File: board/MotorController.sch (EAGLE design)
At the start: 33 parts, among them Q1 IPP80P03P4L-04, Q2 8Mhz, T1 BT139X-600E, U1 ATTINY84-20PU

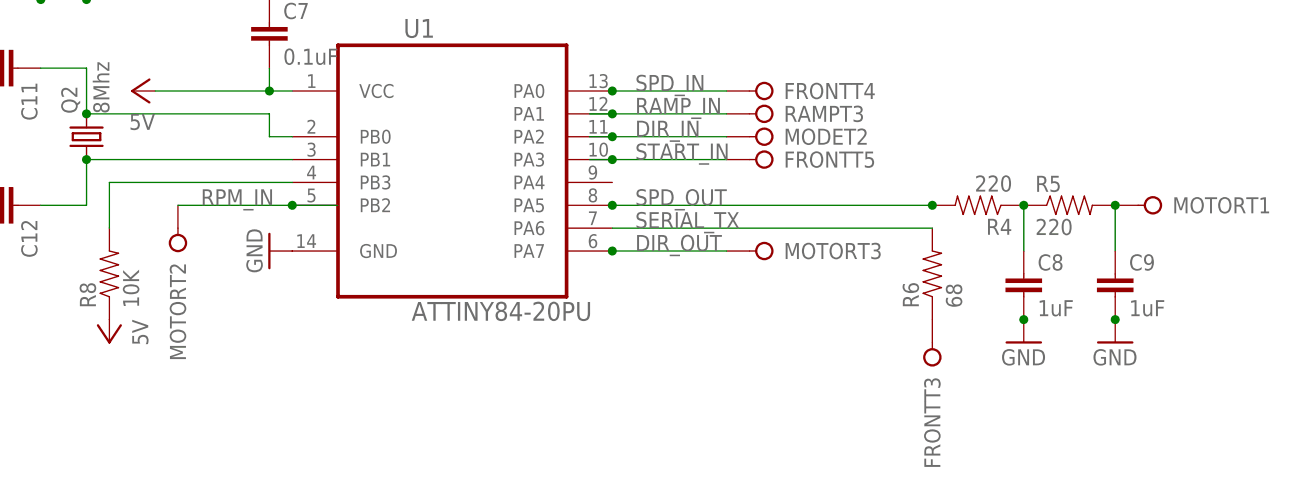
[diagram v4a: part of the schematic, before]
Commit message: Board layout improvements
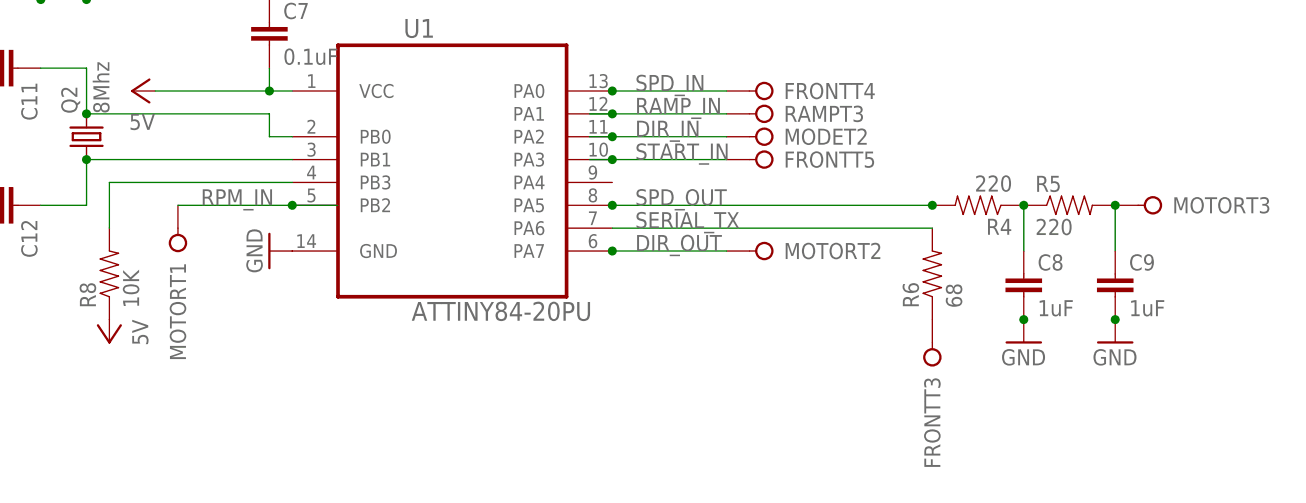
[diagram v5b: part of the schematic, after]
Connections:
- net N$2 renamed RESET
- net DIR_OUT: now also MOTORT2.KL; no longer MOTORT3.KL
- net N$10: now also MOTORT3.KL; no longer MOTORT1.KL
- net RPM_IN: now also MOTORT1.KL; no longer MOTORT2.KL
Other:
- moved on the sheet: MOTORT1, MOTORT2, MOTORT3
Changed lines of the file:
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@@
 <instance part="FRONT" gate="T3" x="106.68" y="-17.78" rot="R90"/>
 <instance part="RAMP" gate="T3" x="88.9" y="10.16" rot="R180"/>
-<instance part="MOTOR" gate="T1" x="132.08" y="0" rot="R180"/>
-<instance part="MOTOR" gate="T2" x="22.86" y="-5.08" rot="R90"/>
-<instance part="MOTOR" gate="T3" x="88.9" y="-5.08" rot="R180"/>
 <instance part="FRONT" gate="T4" x="88.9" y="12.7" rot="R180"/>
 <instance part="FRONT" gate="T5" x="88.9" y="5.08" rot="R180"/>
@@
 <instance part="MOTOR" gate="T4" x="63.5" y="35.56" rot="R90"/>
 <instance part="C1" gate="G$1" x="40.64" y="48.26"/>
+<instance part="MOTOR" gate="T1" x="22.86" y="-5.08" rot="R90"/>
+<instance part="MOTOR" gate="T2" x="88.9" y="-5.08" rot="R180"/>
+<instance part="MOTOR" gate="T3" x="132.08" y="0" rot="R180"/>
 </instances>
 <busses>
@@
 <junction x="35.56" y="0"/>
 <label x="25.4" y="0" size="1.778" layer="95"/>
-<pinref part="MOTOR" gate="T2" pin="KL"/>
+<pinref part="MOTOR" gate="T1" pin="KL"/>
 </segment>
 </net>
@@
 <label x="73.66" y="-5.08" size="1.778" layer="95"/>
 <junction x="71.12" y="-5.08"/>
-<pinref part="MOTOR" gate="T3" pin="KL"/>
+<pinref part="MOTOR" gate="T2" pin="KL"/>
 </segment>
 </net>
@@
 <pinref part="C9" gate="G$1" pin="1"/>
 <wire x1="127" y1="-5.08" x2="127" y2="0" width="0.1524" layer="91"/>
-<pinref part="MOTOR" gate="T1" pin="KL"/>
+<pinref part="MOTOR" gate="T3" pin="KL"/>
 <junction x="127" y="0"/>
 </segment>
@@
 </segment>
 </net>
-<net name="N$2" class="0">
+<net name="RESET" class="0">
 <segment>
 <pinref part="U1" gate="A" pin="PB3"/>

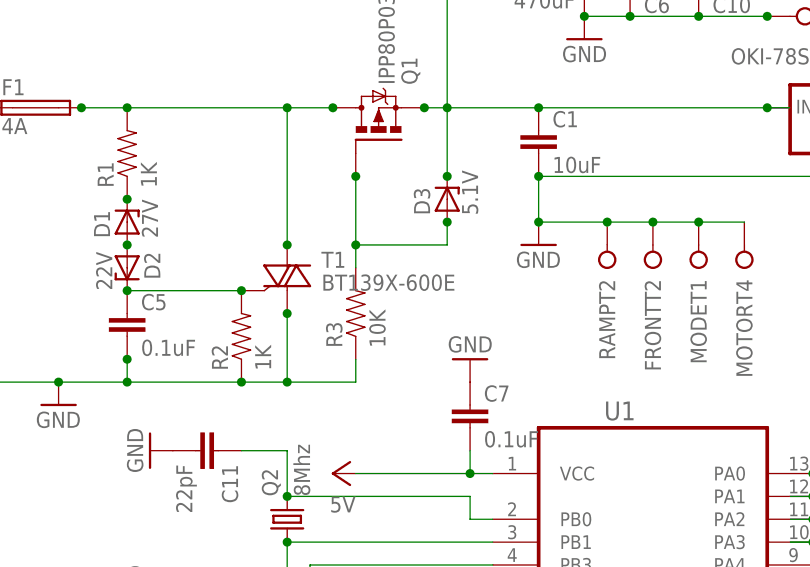
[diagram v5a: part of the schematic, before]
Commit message: Change triac value
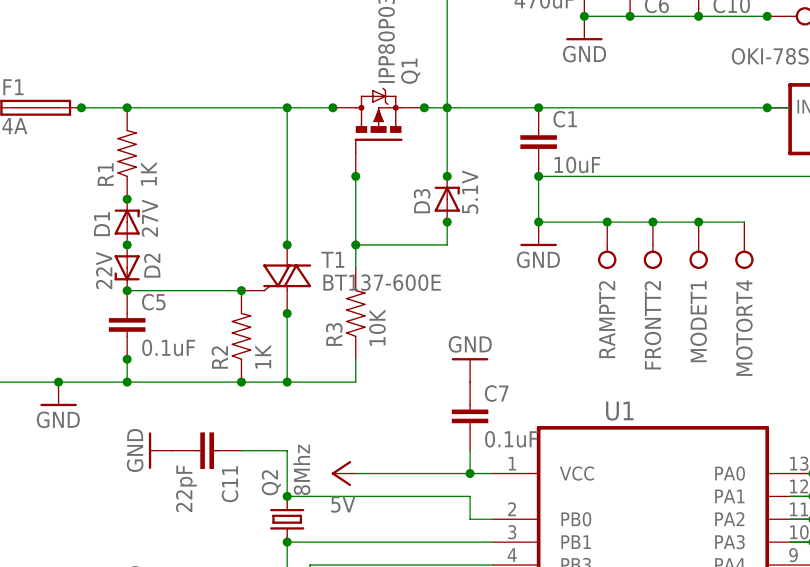
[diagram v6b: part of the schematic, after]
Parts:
- T1: value BT139X-600E -> BT137-600E
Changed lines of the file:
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@@
 <part name="C4" library="SaintGimp" deviceset="CAP-POL" device="-25-14" value="470uF"/>
 <part name="F1" library="SaintGimp" deviceset="FUSE" device="" value="4A"/>
-<part name="T1" library="SaintGimp" deviceset="TRIAC" device="-H" value="BT139X-600E"/>
+<part name="T1" library="SaintGimp" deviceset="TRIAC" device="-H" value="BT137-600E"/>
 <part name="D2" library="SaintGimp" deviceset="ZENER" device="-7.5" value="22V"/>
 <part name="D1" library="SaintGimp" deviceset="ZENER" device="-7.5" value="27V"/>

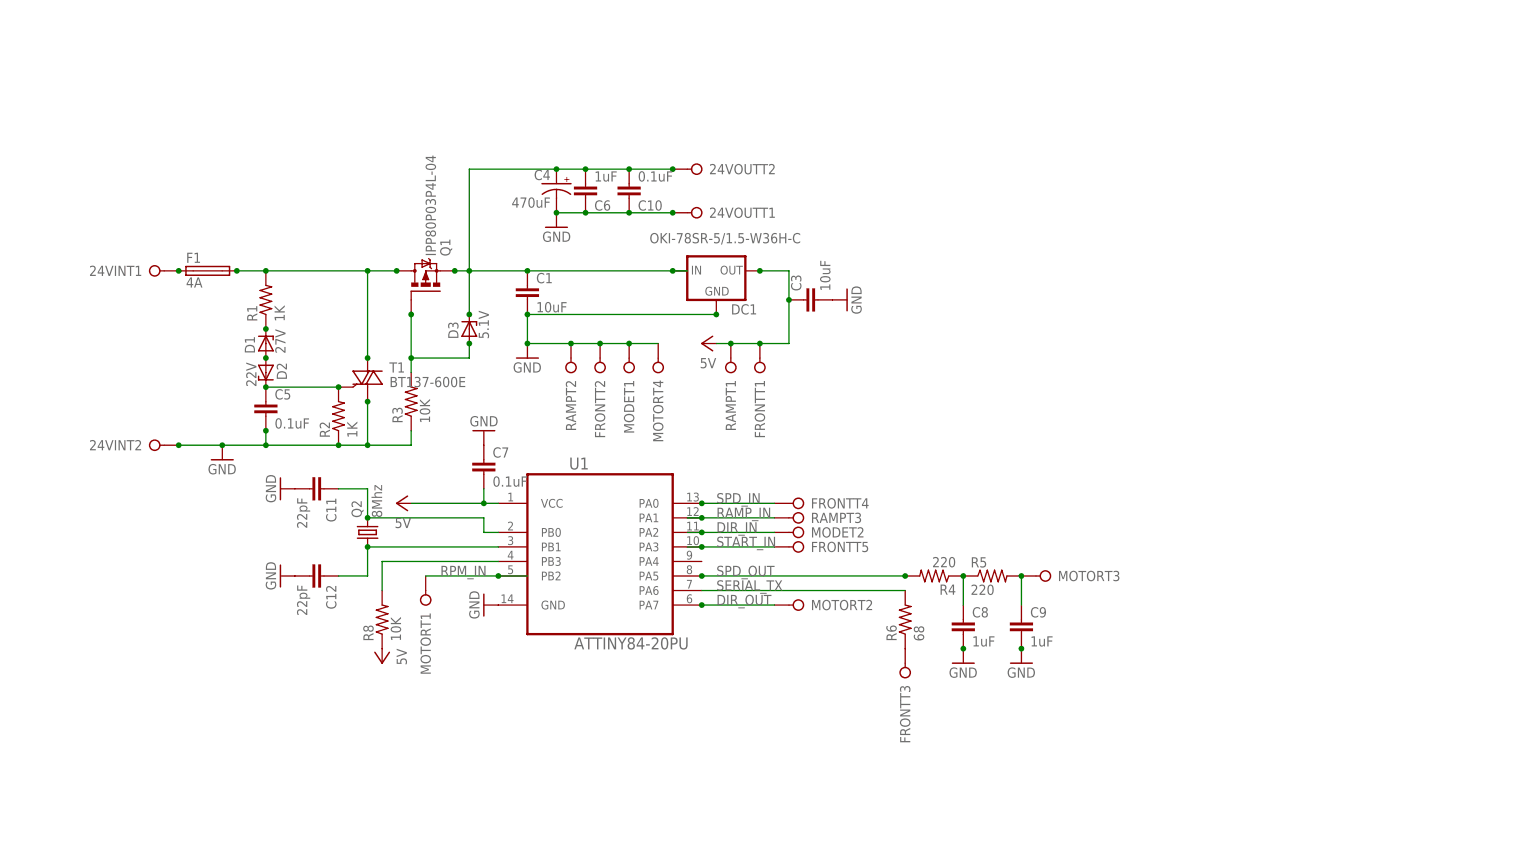
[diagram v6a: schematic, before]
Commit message: Switch to pin headers and ATMega328P
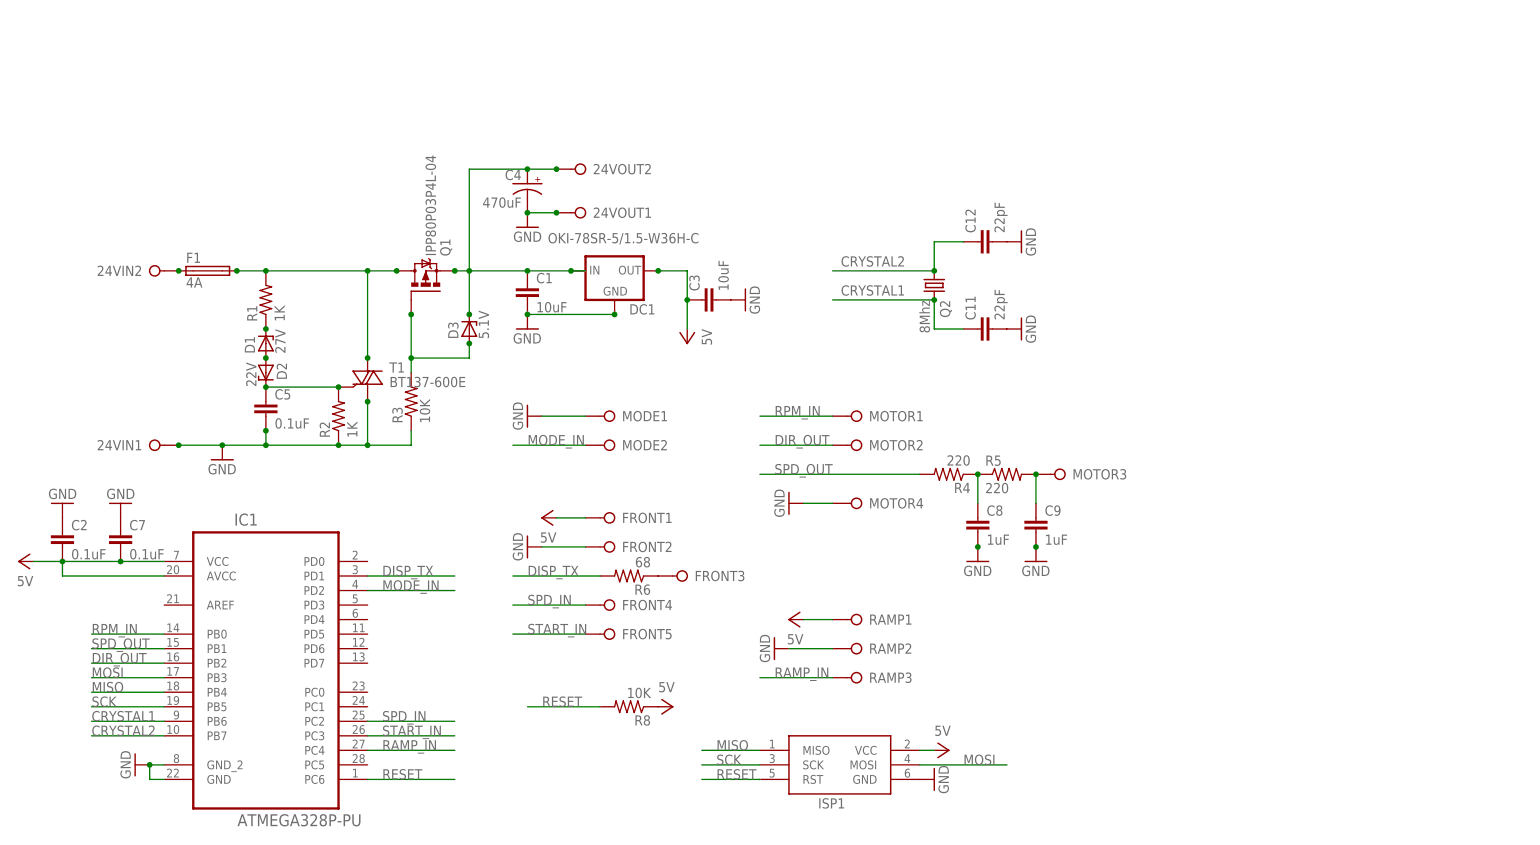
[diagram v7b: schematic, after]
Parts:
- removed C10: 0.1uF, SaintGimp:CAPACITOR-5MM
- removed C6: 1uF, SaintGimp:CAPACITOR-5MM
- removed U1: ATTINY84-20PU, SaintGimp:ATTINY84-20PU
- added C2: 0.1uF, SaintGimp:CAPACITOR-5MM
- added IC1: ATMEGA328P-PU, SaintGimp:ATMEGA328P-PU
- added ISP1: ICSP-HEADER-6, SaintGimp:ICSP-HEADER-6
- 24VIN, 24VOUT, MODE: value SCREW-TERM-2 -> PINHD-1X2; device SaintGimp:SCREW-TERM-2 -> SaintGimp:PINHD-1X2
- FRONT: value SCREW-TERM-5 -> PINHD-1X5; device SaintGimp:SCREW-TERM-5 -> SaintGimp:PINHD-1X5
- MOTOR: value SCREW-TERM-4 -> PINHD-1X4; device SaintGimp:SCREW-TERM-4 -> SaintGimp:PINHD-1X4
- RAMP: value SCREW-TERM-3 -> PINHD-1X3; device SaintGimp:SCREW-TERM-3 -> SaintGimp:PINHD-1X3
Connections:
- removed net DIR_IN: MODET2.KL, U1.PA2
- removed net N$12: C12.1, Q2.1, U1.PB1
- removed net N$13: C11.1, Q2.2, U1.PB0
- removed net SERIAL_TX: R6.2, U1.PA6
- new net CRYSTAL1: C11.1, IC1.PB6, Q2.2
- new net CRYSTAL2: C12.1, IC1.PB7, Q2.1
- new net DISP_TX: IC1.PD1, R6.2
- new net MISO: IC1.PB4, ISP1.MISO
- new net MODE_IN: IC1.PD2, MODE2.KL
- new net MOSI: IC1.PB3, ISP1.MOSI
- new net SCK: IC1.PB5, ISP1.SCK
- net 24V-PROTECTED: now also 24VOUT2.KL; no longer 24VOUTT2.KL, C10.2, C6.2
- net DIR_OUT: now also IC1.PB2, MOTOR2.KL; no longer MOTORT2.KL, U1.PA7
- net GND: now also 24VIN1.KL, 24VOUT1.KL, C2.1, FRONT2.KL, IC1.GND, IC1.GND_2, ISP1.GND, MODE1.KL, MOTOR4.KL, RAMP2.KL; no longer 24VINT2.KL, 24VOUTT1.KL, C10.1, C6.1, FRONTT2.KL, MODET1.KL, MOTORT4.KL, RAMPT2.KL, U1.GND
- net N$10: now also MOTOR3.KL; no longer MOTORT3.KL
- net N$3: now also 24VIN2.KL; no longer 24VINT1.KL
- net N$8: now also FRONT3.KL; no longer FRONTT3.KL
- net RAMP_IN: now also IC1.PC4, RAMP3.KL; no longer RAMPT3.KL, U1.PA1
- net RESET: now also IC1.PC6, ISP1.RST; no longer U1.PB3
- net RPM_IN: now also IC1.PB0, MOTOR1.KL; no longer MOTORT1.KL, U1.PB2
- net SPD_IN: now also FRONT4.KL, IC1.PC2; no longer FRONTT4.KL, U1.PA0
- net SPD_OUT: now also IC1.PB1; no longer U1.PA5
- net START_IN: now also FRONT5.KL, IC1.PC3; no longer FRONTT5.KL, U1.PA3
- net VCC: now also C2.2, FRONT1.KL, IC1.AVCC, IC1.VCC, ISP1.VCC, RAMP1.KL; no longer FRONTT1.KL, RAMPT1.KL, U1.VCC
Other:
- moved on the sheet: C11, C12, C3, C4, C7, C8, C9, DC1, Q2, R4, R5, R6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

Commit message: Version 3, many changes
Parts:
- added FOOT: PINHD-1X2BIG, SaintGimp:PINHD-1X2BIG
- added SIDE_EXP: PINHD-1X3BIG, SaintGimp:PINHD-1X3BIG
- 24VIN, 24VOUT, MODE: value PINHD-1X2 -> PINHD-1X2BIG; device SaintGimp:PINHD-1X2 -> SaintGimp:PINHD-1X2BIG
- C11, C12: value 22pF -> 20pF
- C2, C5, C7, C8, C9: device SaintGimp:CAPACITOR-5MM -> SaintGimp:CAPACITOR-2.5MM
- C4: value 470uF -> 1000uF
- D3: value 5.1V -> 10V
- FRONT: value PINHD-1X5 -> PINHD-1X7BIG; device SaintGimp:PINHD-1X5 -> SaintGimp:PINHD-1X7BIG
- MOTOR: value PINHD-1X4 -> PINHD-1X4BIG; device SaintGimp:PINHD-1X4 -> SaintGimp:PINHD-1X4BIG
- Q2: value 8Mhz -> 16Mhz
- RAMP: value PINHD-1X3 -> PINHD-1X3BIG; device SaintGimp:PINHD-1X3 -> SaintGimp:PINHD-1X3BIG
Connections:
- new net EXP1: IC1.PC4, SIDE_EXP3.KL
- new net EXP2: FRONT4.KL, IC1.PC1
- new net EXP3: FRONT3.KL, IC1.PC0
- net 24V-PROTECTED: now also 24VOUT1.KL; no longer 24VOUT2.KL
- net GND: now also 24VOUT2.KL, FOOT1.KL, SIDE_EXP2.KL; no longer 24VOUT1.KL
- net N$8: now also FRONT5.KL; no longer FRONT3.KL
- net RAMP_IN: now also IC1.PC5; no longer IC1.PC4
- net SPD_IN: now also FRONT6.KL; no longer FRONT4.KL
- net START_IN: now also FOOT2.KL, FRONT7.KL; no longer FRONT5.KL
- net VCC: now also SIDE_EXP1.KL
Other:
- moved on the sheet: 24VOUT1, 24VOUT2, C11, C12, FRONT3, FRONT5, Q2, R6, R8
